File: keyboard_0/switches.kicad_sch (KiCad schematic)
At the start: 135 parts, among them J1 Conn_02x12_Top_Bottom

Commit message: update to use prebuilt mcu pcb
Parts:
- removed J1: Conn_02x12_Top_Bottom, PCM_marbastlib-xp-promicroish:Elite-C_AH_Reversible, symbol Connector_Generic:Conn_02x12_Top_Bottom
- added D29: D_Small, Diode_SMD:D_SOD-323_HandSoldering, symbol Device:D_Small
- added MX29: MX_SW_HS, PCM_Switch_Keyboard_Cherry_MX:SW_Cherry_MX_PCB_1.00u, symbol PCM_marbastlib-mx:MX_SW_HS_CPG151101S11
- added S4: MX_stab, PCM_marbastlib-mx:STAB_MX_P_2.25u, symbol PCM_marbastlib-mx:MX_stab
- D1, D10, D11, D12, D13, D14, D15, D16, D17, D18, D19, D2, D20, D21, D22, D23, D24, D25, D26, D27, D28, D3, D30, D31, D32, D33, D34, D35, D36, D37, D38, D39, D4, D40, D41, D42, D43, D44, D45, D46, D47, D48, D49, D5, D50, D51, D52, D53, D54, D55, D56, D57, D58, D59, D6, D60, D61, D62, D63, D64, D65, D66, D7, D8, D9: footprint Diode_SMD:D_SOD-323 -> Diode_SMD:D_SOD-323_HandSoldering
- S1: footprint PCM_marbastlib-mx:STAB_MX_P_6.25u -> PCM_marbastlib-mx:STAB_MX_P_2.25u
- S2: footprint PCM_marbastlib-mx:STAB_MX_P_2.25u -> PCM_marbastlib-mx:STAB_MX_P_6.25u
- S5: footprint PCM_marbastlib-mx:STAB_MX_P_2.25u -> PCM_marbastlib-mx:STAB_MX_P_2u
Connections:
- net COL14: now also MX29.1
- net ROW0: now also D29.1 (K)
- new net: D29.2 (A), MX29.2
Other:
- title: (none) -> Switch Matrix
- moved on the sheet: D1, D10, D11, D12, D13, D14, D15, D16, D17, D18, D19, D2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

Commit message: latest changes - incomplete routing
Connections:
- net ROW0: no longer D29.1 (K)
- net ROW1: now also D29.1 (K)
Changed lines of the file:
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@@
 	)
 	(junction
-		(at 228.6 68.58)
-		(diameter 0)
-		(color 0 0 0 0)
-	)
-	(junction
 		(at 172.72 58.42)
 		(diameter 0)
@@
 	)
 	(junction
+		(at 228.6 86.36)
+		(diameter 0)
+		(color 0 0 0 0)
+	)
+	(junction
 		(at 109.22 58.42)
 		(diameter 0)
@@
 	(wire
 		(pts
-			(xy 231.14 86.36) (xy 231.14 68.58)
-		)
-		(stroke
-			(width 0)
-			(type default)
-		)
-	)
-	(wire
-		(pts
 			(xy 210.82 44.45) (xy 210.82 58.42)
 		)
@@
 	(wire
 		(pts
-			(xy 241.3 86.36) (xy 231.14 86.36)
-		)
-		(stroke
-			(width 0)
-			(type default)
-		)
-	)
-	(wire
-		(pts
 			(xy 76.2 102.87) (xy 88.9 102.87)
 		)
@@
 	(wire
 		(pts
-			(xy 231.14 68.58) (xy 228.6 68.58)
-		)
-		(stroke
-			(width 0)
-			(type default)
-		)
-	)
-	(wire
-		(pts
 			(xy 152.4 86.36) (xy 165.1 86.36)
 		)
@@
 	(wire
 		(pts
+			(xy 228.6 86.36) (xy 241.3 86.36)
+		)
+		(stroke
+			(width 0)
+			(type default)
+		)
+	)
+	(wire
+		(pts
 			(xy 83.82 92.71) (xy 83.82 110.49)
 		)
@@
 				)
 			)
+			(project "switches"
+				(path "/d43833e6-42f1-45e5-83d6-28baccbabb57"
+					(reference "S3")
+					(unit 1)
+				)
+			)
 		)
 	)
@@
 				)
 			)
+			(project "switches"
+				(path "/d43833e6-42f1-45e5-83d6-28baccbabb57"
+					(reference "S4")
+					(unit 1)
+				)
+			)
 		)
 	)
@@
 				)
 			)
+			(project "switches"
+				(path "/d43833e6-42f1-45e5-83d6-28baccbabb57"
+					(reference "D29")
+					(unit 1)
+				)
+			)
 		)
 	)
@@
 				)
 			)
+			(project "switches"
+				(path "/d43833e6-42f1-45e5-83d6-28baccbabb57"
+					(reference "S1")
+					(unit 1)
+				)
+			)
 		)
 	)
@@
 				)
 			)
+			(project "switches"
+				(path "/d43833e6-42f1-45e5-83d6-28baccbabb57"
+					(reference "S2")
+					(unit 1)
+				)
+			)
 		)
 	)
@@
 				)
 			)
+			(project "switches"
+				(path "/d43833e6-42f1-45e5-83d6-28baccbabb57"
+					(reference "S5")
+					(unit 1)
+				)
+			)
 		)
 	)
@@
 					(reference "MX29")
 					(unit 1)
+				)
+			)
+			(project "switches"
+				(path "/d43833e6-42f1-45e5-83d6-28baccbabb57"
+					(reference "MX29")
+					(unit 1)

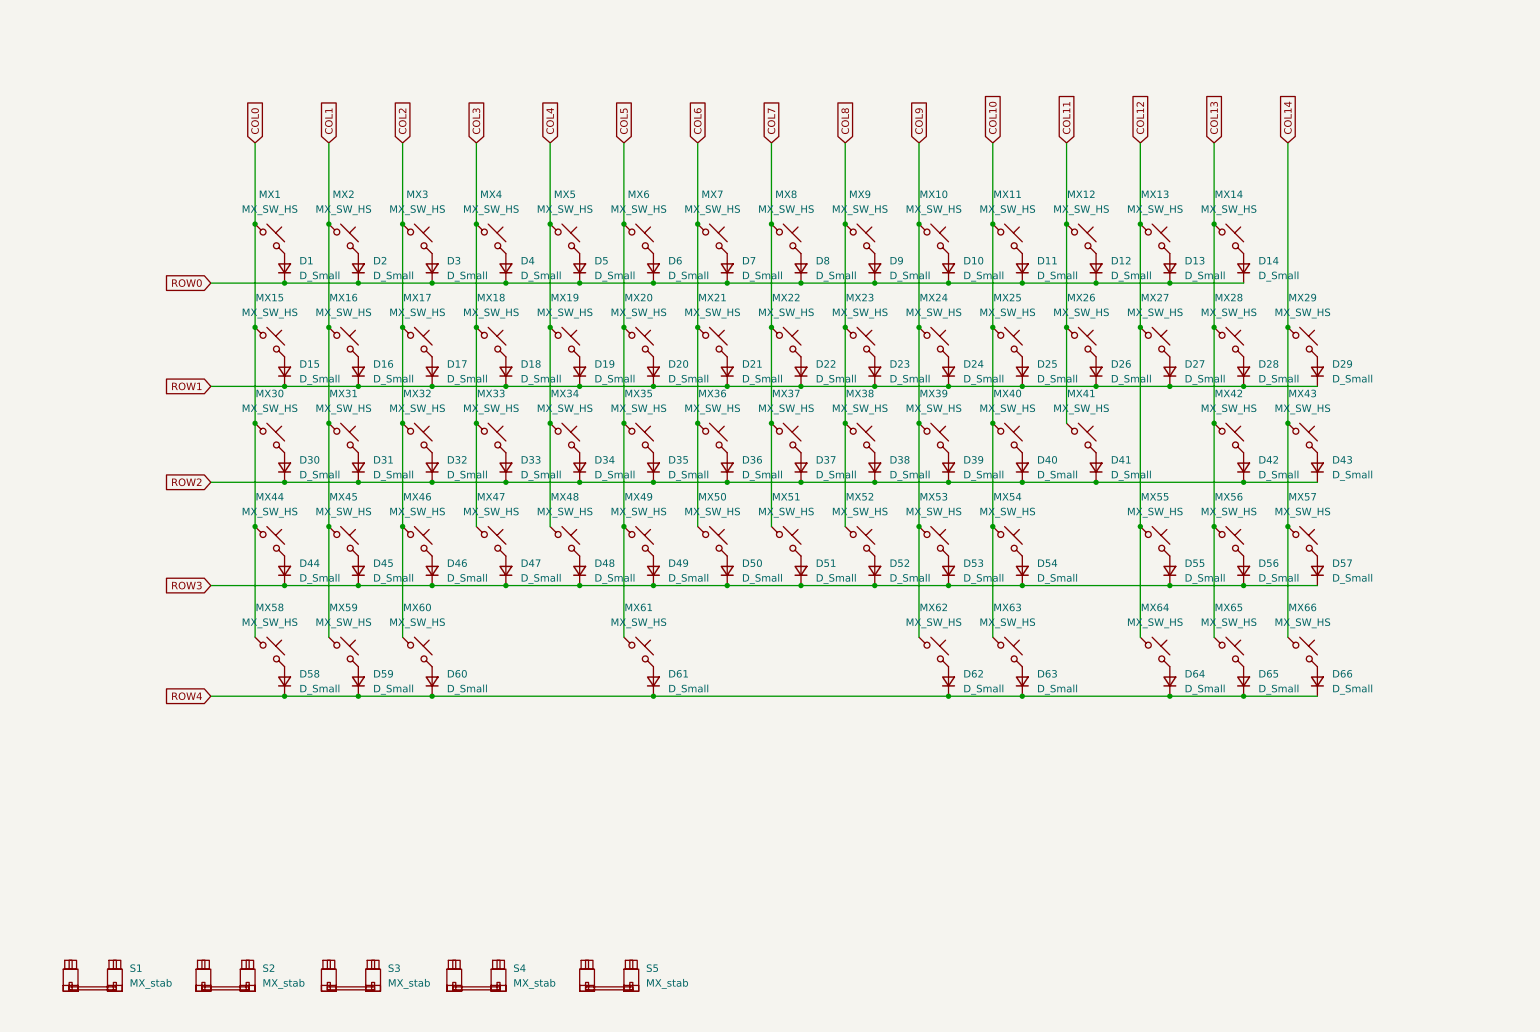
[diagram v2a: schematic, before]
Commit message: connect rest of switches and bring in aux components
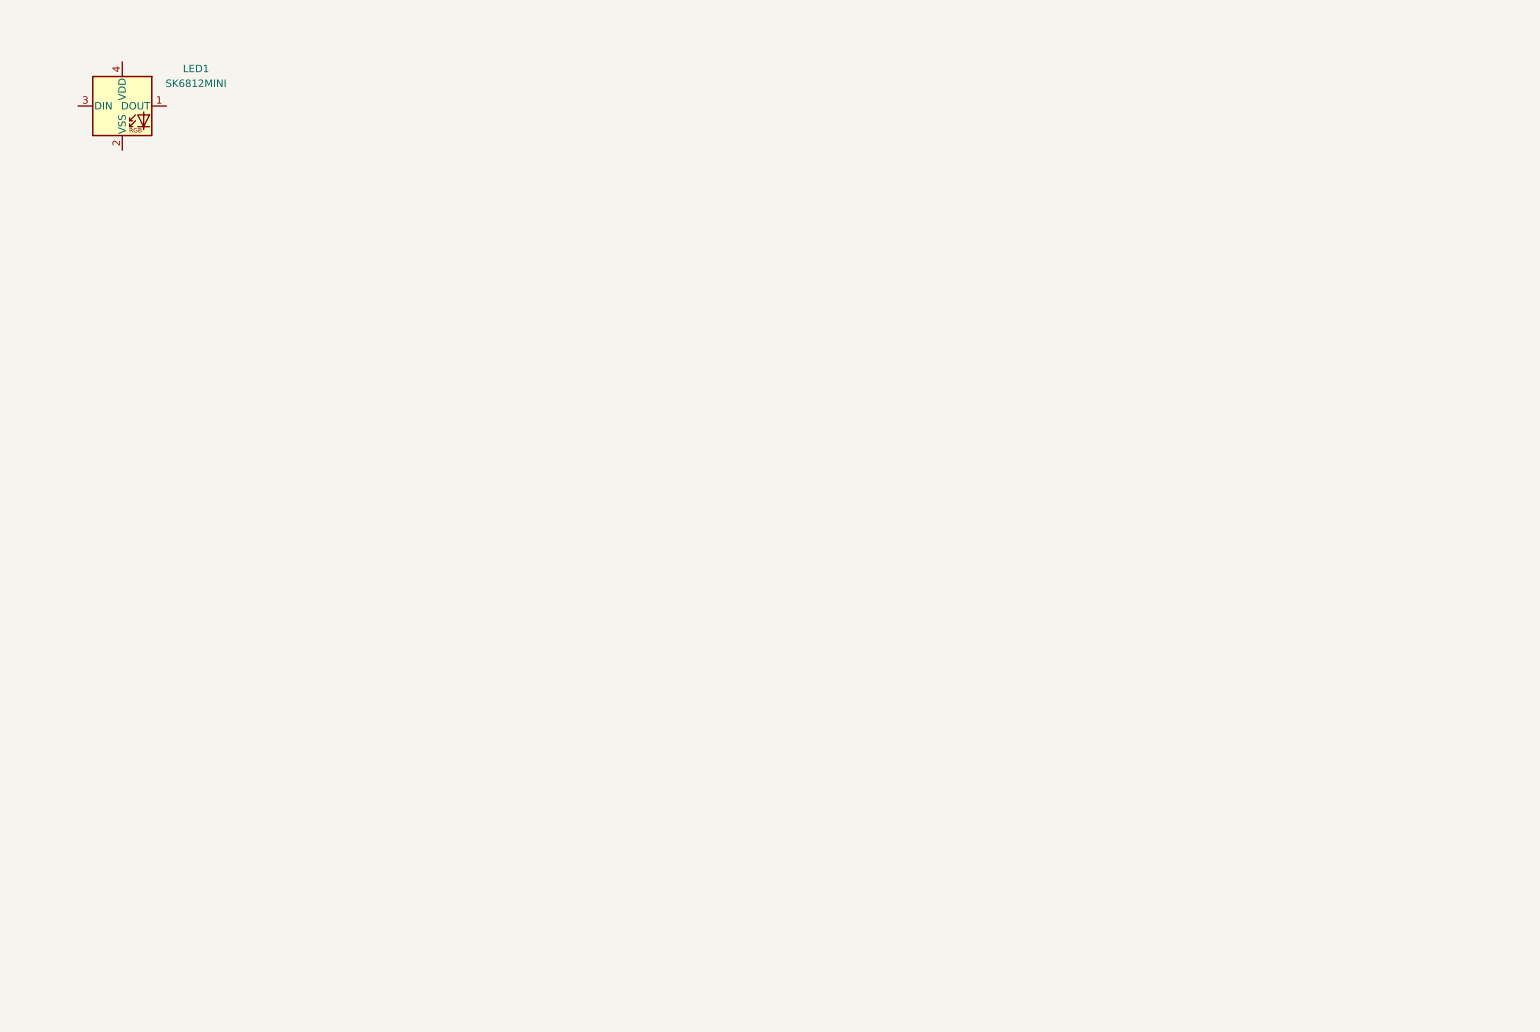
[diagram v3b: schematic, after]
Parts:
- removed D1, D10, D11, D12, D13, D14, D15, D16, D17, D18, D19, D2, D20, D21, D22, D23, D24, D25, D26, D27, D28, D29, D3, D30, D31, D32, D33, D34, D35, D36, D37, D38, D39, D4, D40, D41, D42, D43, D44, D45, D46, D47, D48, D49, D5, D50, D51, D52, D53, D54, D55, D56, D57, D58, D59, D6, D60, D61, D62, D63, D64, D65, D66, D7, D8, D9: D_Small, Diode_SMD:D_SOD-323_HandSoldering, symbol Device:D_Small
- removed MX1, MX10, MX11, MX12, MX13, MX16, MX17, MX18, MX19, MX2, MX20, MX21, MX22, MX23, MX24, MX25, MX26, MX27, MX29, MX3, MX31, MX32, MX33, MX34, MX35, MX36, MX37, MX38, MX39, MX4, MX40, MX41, MX43, MX45, MX46, MX47, MX48, MX49, MX5, MX50, MX51, MX52, MX53, MX54, MX56, MX57, MX6, MX64, MX65, MX66, MX7, MX8, MX9: MX_SW_HS, PCM_Switch_Keyboard_Cherry_MX:SW_Cherry_MX_PCB_1.00u, symbol PCM_marbastlib-mx:MX_SW_HS_CPG151101S11
- removed MX14, MX55: MX_SW_HS, PCM_Switch_Keyboard_Cherry_MX:SW_Cherry_MX_PCB_2.00u, symbol PCM_marbastlib-mx:MX_SW_HS_CPG151101S11
- removed MX15, MX28: MX_SW_HS, PCM_Switch_Keyboard_Cherry_MX:SW_Cherry_MX_PCB_1.50u, symbol PCM_marbastlib-mx:MX_SW_HS_CPG151101S11
- removed MX30: MX_SW_HS, PCM_Switch_Keyboard_Cherry_MX:SW_Cherry_MX_PCB_1.75u, symbol PCM_marbastlib-mx:MX_SW_HS_CPG151101S11
- removed MX42, MX44: MX_SW_HS, PCM_Switch_Keyboard_Cherry_MX:SW_Cherry_MX_PCB_2.25u, symbol PCM_marbastlib-mx:MX_SW_HS_CPG151101S11
- removed MX58, MX59, MX60, MX62, MX63: MX_SW_HS, PCM_Switch_Keyboard_Cherry_MX:SW_Cherry_MX_PCB_1.25u, symbol PCM_marbastlib-mx:MX_SW_HS_CPG151101S11
- removed MX61: MX_SW_HS, PCM_Switch_Keyboard_Cherry_MX:SW_Cherry_MX_PCB_6.25u, symbol PCM_marbastlib-mx:MX_SW_HS_CPG151101S11
- removed S1, S4: MX_stab, PCM_marbastlib-mx:STAB_MX_P_2.25u, symbol PCM_marbastlib-mx:MX_stab
- removed S2: MX_stab, PCM_marbastlib-mx:STAB_MX_P_6.25u, symbol PCM_marbastlib-mx:MX_stab
- removed S3, S5: MX_stab, PCM_marbastlib-mx:STAB_MX_P_2u, symbol PCM_marbastlib-mx:MX_stab
- added LED1: SK6812MINI, LED_SMD:LED_SK6812MINI_PLCC4_3.5x3.5mm_P1.75mm, symbol LED:SK6812MINI

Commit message: bring back switches and separate sub sheets
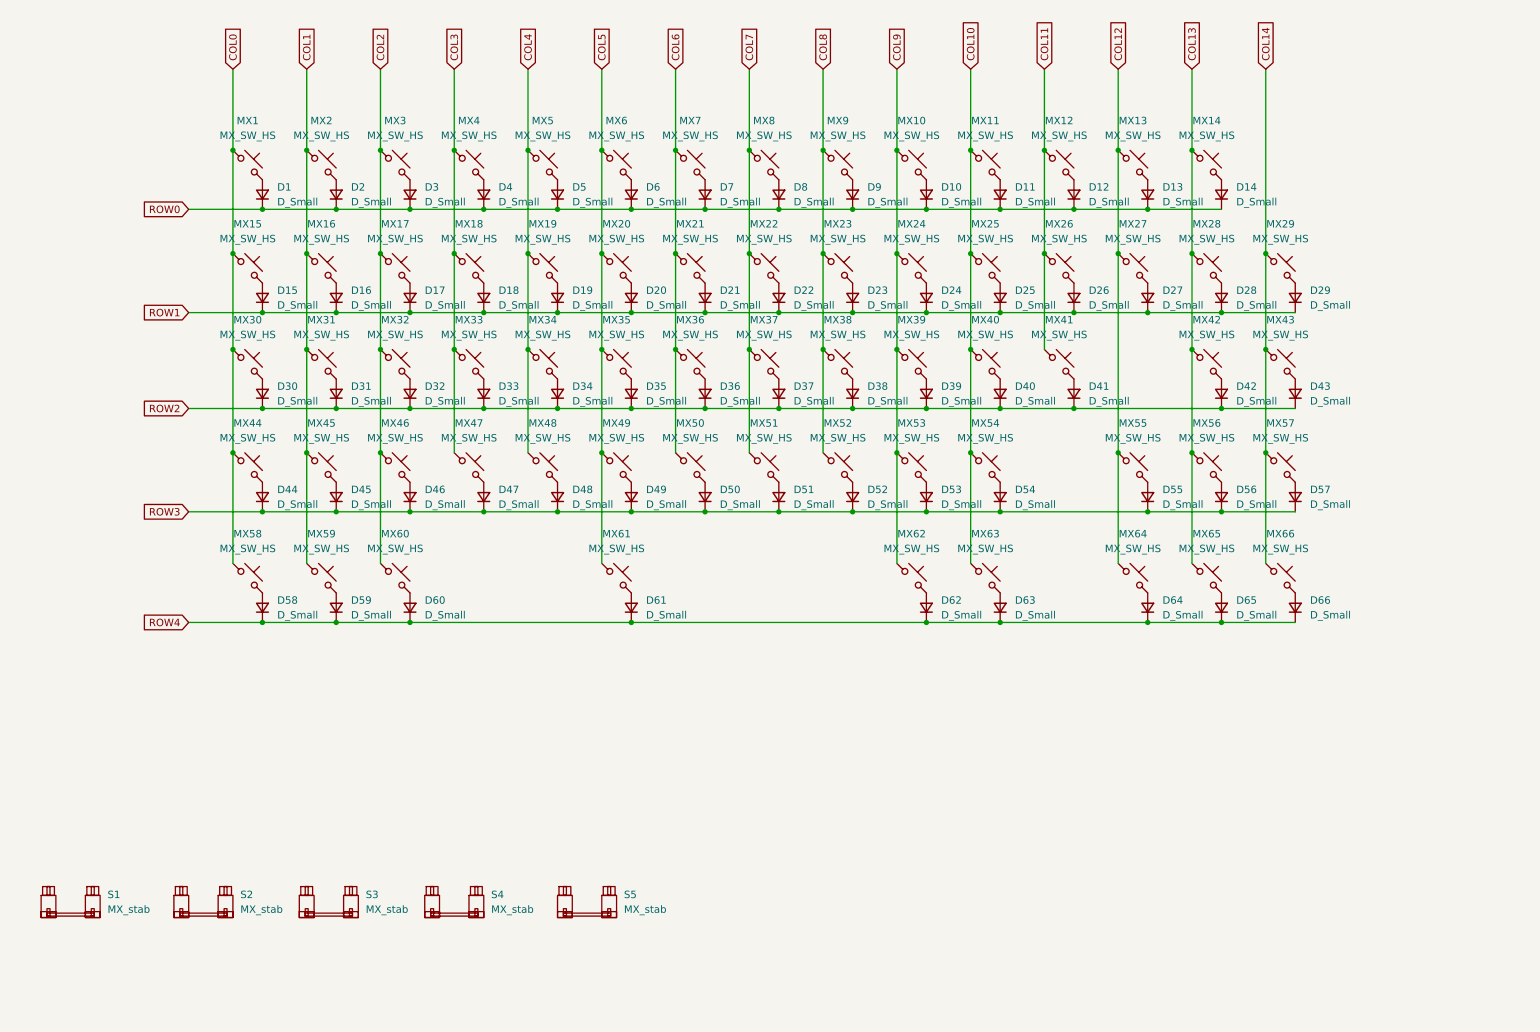
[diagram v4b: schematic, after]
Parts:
- removed LED1: SK6812MINI, LED_SMD:LED_SK6812MINI_PLCC4_3.5x3.5mm_P1.75mm, symbol LED:SK6812MINI
- added D1, D10, D11, D12, D13, D14, D15, D16, D17, D18, D19, D2, D20, D21, D22, D23, D24, D25, D26, D27, D28, D29, D3, D30, D31, D32, D33, D34, D35, D36, D37, D38, D39, D4, D40, D41, D42, D43, D44, D45, D46, D47, D48, D49, D5, D50, D51, D52, D53, D54, D55, D56, D57, D58, D59, D6, D60, D61, D62, D63, D64, D65, D66, D7, D8, D9: D_Small, Diode_SMD:D_SOD-323_HandSoldering, symbol Device:D_Small
- added MX1, MX10, MX11, MX12, MX13, MX16, MX17, MX18, MX19, MX2, MX20, MX21, MX22, MX23, MX24, MX25, MX26, MX27, MX29, MX3, MX31, MX32, MX33, MX34, MX35, MX36, MX37, MX38, MX39, MX4, MX40, MX41, MX43, MX45, MX46, MX47, MX48, MX49, MX5, MX50, MX51, MX52, MX53, MX54, MX56, MX57, MX6, MX64, MX65, MX66, MX7, MX8, MX9: MX_SW_HS, PCM_Switch_Keyboard_Cherry_MX:SW_Cherry_MX_PCB_1.00u, symbol PCM_marbastlib-mx:MX_SW_HS_CPG151101S11
- added MX14, MX55: MX_SW_HS, PCM_Switch_Keyboard_Cherry_MX:SW_Cherry_MX_PCB_2.00u, symbol PCM_marbastlib-mx:MX_SW_HS_CPG151101S11
- added MX15, MX28: MX_SW_HS, PCM_Switch_Keyboard_Cherry_MX:SW_Cherry_MX_PCB_1.50u, symbol PCM_marbastlib-mx:MX_SW_HS_CPG151101S11
- added MX30: MX_SW_HS, PCM_Switch_Keyboard_Cherry_MX:SW_Cherry_MX_PCB_1.75u, symbol PCM_marbastlib-mx:MX_SW_HS_CPG151101S11
- added MX42, MX44: MX_SW_HS, PCM_Switch_Keyboard_Cherry_MX:SW_Cherry_MX_PCB_2.25u, symbol PCM_marbastlib-mx:MX_SW_HS_CPG151101S11
- added MX58, MX59, MX60, MX62, MX63: MX_SW_HS, PCM_Switch_Keyboard_Cherry_MX:SW_Cherry_MX_PCB_1.25u, symbol PCM_marbastlib-mx:MX_SW_HS_CPG151101S11
- added MX61: MX_SW_HS, PCM_Switch_Keyboard_Cherry_MX:SW_Cherry_MX_PCB_6.25u, symbol PCM_marbastlib-mx:MX_SW_HS_CPG151101S11
- added S1, S4: MX_stab, PCM_marbastlib-mx:STAB_MX_P_2.25u, symbol PCM_marbastlib-mx:MX_stab
- added S2: MX_stab, PCM_marbastlib-mx:STAB_MX_P_6.25u, symbol PCM_marbastlib-mx:MX_stab
- added S3, S5: MX_stab, PCM_marbastlib-mx:STAB_MX_P_2u, symbol PCM_marbastlib-mx:MX_stab
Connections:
- new net: D16.2 (A), MX16.2
- new net: D55.2 (A), MX55.2
- new net: D1.2 (A), MX1.2
- new net: D40.2 (A), MX40.2
- new net: D24.2 (A), MX24.2
- new net: D36.2 (A), MX36.2
- new net: D11.2 (A), MX11.2
- new net: D54.2 (A), MX54.2
- new net: D63.2 (A), MX63.2
- new net: D14.2 (A), MX14.2
- new net: D61.2 (A), MX61.2
- new net: D6.2 (A), MX6.2
- new net: D56.2 (A), MX56.2
- new net: D66.2 (A), MX66.2
- new net: D34.2 (A), MX34.2
- new net: D31.2 (A), MX31.2
- new net: D22.2 (A), MX22.2
- new net: D33.2 (A), MX33.2
- new net: D23.2 (A), MX23.2
- new net: D20.2 (A), MX20.2
- new net: D2.2 (A), MX2.2
- new net: D13.2 (A), MX13.2
- new net: D10.2 (A), MX10.2
- new net: D18.2 (A), MX18.2
- new net: D62.2 (A), MX62.2
- new net: D53.2 (A), MX53.2
- new net: D50.2 (A), MX50.2
- new net: D59.2 (A), MX59.2
- new net: D47.2 (A), MX47.2
- new net: D38.2 (A), MX38.2
- new net: D3.2 (A), MX3.2
- new net: D30.2 (A), MX30.2
- new net: D43.2 (A), MX43.2
- new net: D32.2 (A), MX32.2
- new net: D37.2 (A), MX37.2
- new net: D46.2 (A), MX46.2
- new net: D52.2 (A), MX52.2
- new net: D25.2 (A), MX25.2
- new net: D9.2 (A), MX9.2
- new net: D15.2 (A), MX15.2
- new net: D12.2 (A), MX12.2
- new net: D49.2 (A), MX49.2
- new net: D42.2 (A), MX42.2
- new net: D19.2 (A), MX19.2
- new net: D17.2 (A), MX17.2
- new net: D51.2 (A), MX51.2
- new net: D65.2 (A), MX65.2
- new net: D41.2 (A), MX41.2
- new net: D29.2 (A), MX29.2
- new net: D39.2 (A), MX39.2
- new net: D45.2 (A), MX45.2
- new net: D7.2 (A), MX7.2
- new net: D28.2 (A), MX28.2
- new net: D57.2 (A), MX57.2
- new net: D4.2 (A), MX4.2
- new net: D21.2 (A), MX21.2
- new net: D26.2 (A), MX26.2
- new net: D48.2 (A), MX48.2
- new net: D64.2 (A), MX64.2
- new net: D27.2 (A), MX27.2
- new net: D5.2 (A), MX5.2
- new net: D58.2 (A), MX58.2
- new net: D60.2 (A), MX60.2
- new net: D44.2 (A), MX44.2
- new net: D8.2 (A), MX8.2
- new net: D35.2 (A), MX35.2
- new net COL0: MX1.1, MX15.1, MX30.1, MX44.1, MX58.1
- new net COL1: MX16.1, MX2.1, MX31.1, MX45.1, MX59.1
- new net COL10: MX11.1, MX25.1, MX40.1, MX54.1, MX63.1
- new net COL11: MX12.1, MX26.1, MX41.1
- new net COL12: MX13.1, MX27.1, MX55.1, MX64.1
- new net COL13: MX14.1, MX28.1, MX42.1, MX56.1, MX65.1
- new net COL14: MX29.1, MX43.1, MX57.1, MX66.1
- new net COL2: MX17.1, MX3.1, MX32.1, MX46.1, MX60.1
- new net COL3: MX18.1, MX33.1, MX4.1, MX47.1
- new net COL4: MX19.1, MX34.1, MX48.1, MX5.1
- new net COL5: MX20.1, MX35.1, MX49.1, MX6.1, MX61.1
- new net COL6: MX21.1, MX36.1, MX50.1, MX7.1
- new net COL7: MX22.1, MX37.1, MX51.1, MX8.1
- new net COL8: MX23.1, MX38.1, MX52.1, MX9.1
- new net COL9: MX10.1, MX24.1, MX39.1, MX53.1, MX62.1
- new net ROW0: D1.1 (K), D10.1 (K), D11.1 (K), D12.1 (K), D13.1 (K), D14.1 (K), D2.1 (K), D3.1 (K), D4.1 (K), D5.1 (K), D6.1 (K), D7.1 (K), D8.1 (K), D9.1 (K)
- new net ROW1: D15.1 (K), D16.1 (K), D17.1 (K), D18.1 (K), D19.1 (K), D20.1 (K), D21.1 (K), D22.1 (K), D23.1 (K), D24.1 (K), D25.1 (K), D26.1 (K), D27.1 (K), D28.1 (K), D29.1 (K)
- new net ROW2: D30.1 (K), D31.1 (K), D32.1 (K), D33.1 (K), D34.1 (K), D35.1 (K), D36.1 (K), D37.1 (K), D38.1 (K), D39.1 (K), D40.1 (K), D41.1 (K), D42.1 (K), D43.1 (K)
- new net ROW3: D44.1 (K), D45.1 (K), D46.1 (K), D47.1 (K), D48.1 (K), D49.1 (K), D50.1 (K), D51.1 (K), D52.1 (K), D53.1 (K), D54.1 (K), D55.1 (K), D56.1 (K), D57.1 (K)
- new net ROW4: D58.1 (K), D59.1 (K), D60.1 (K), D61.1 (K), D62.1 (K), D63.1 (K), D64.1 (K), D65.1 (K), D66.1 (K)
